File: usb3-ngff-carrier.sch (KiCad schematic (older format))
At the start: 44 parts, among them J1 692221030100, J2 2199119-3, J3 Jack-DC, J4 693043020611, J5 Conn_01x03_Male, SW1 KMR221GLFS, U1 TPS82130SILR

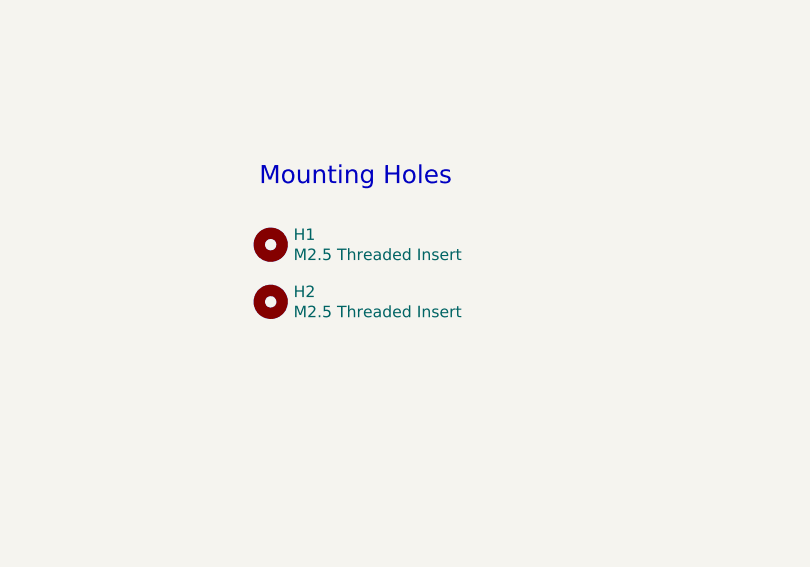
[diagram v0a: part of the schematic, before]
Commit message: Change: SIM holder
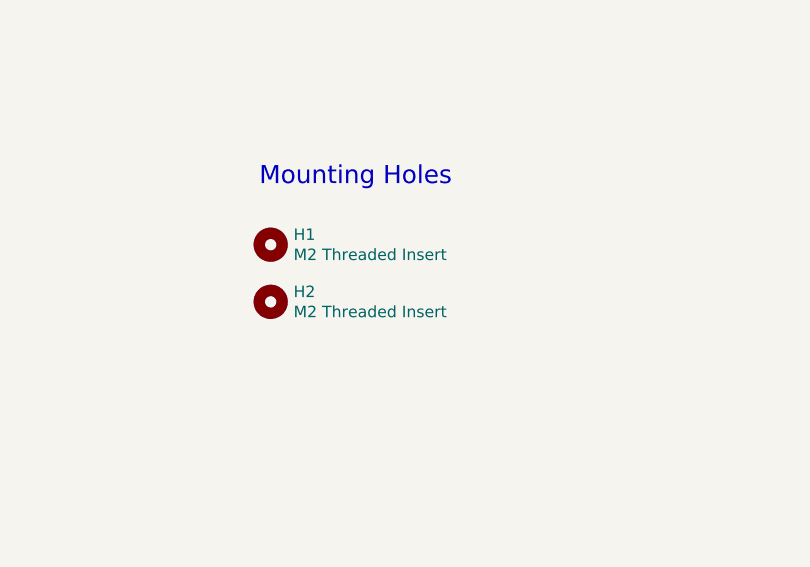
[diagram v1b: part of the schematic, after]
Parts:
- H1, H2: value M2.5 Threaded Insert -> M2 Threaded Insert
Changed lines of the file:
@@
 P 5200 3750
 F 0 "H1" H 5300 3794 50  0000 L CNN
-F 1 "M2.5 Threaded Insert" H 5300 3706 50  0000 L CNN
+F 1 "M2 Threaded Insert" H 5300 3706 50  0000 L CNN
 F 2 "footprint:9774015243RStandoff" H 5200 3750 50  0001 C CNN
 F 3 "https://www.mouser.co.uk/datasheet/2/445/9774015243R-1728818.pdf" H 5200 3750 50  0001 C CNN
@@
 P 5200 4000
 F 0 "H2" H 5300 4044 50  0000 L CNN
-F 1 "M2.5 Threaded Insert" H 5300 3956 50  0000 L CNN
+F 1 "M2 Threaded Insert" H 5300 3956 50  0000 L CNN
 F 2 "footprint:9774015243RStandoff" H 5200 4000 50  0001 C CNN
 F 3 "https://www.mouser.co.uk/datasheet/2/445/9774015243R-1728818.pdf" H 5200 4000 50  0001 C CNN

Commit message: Add: README, BOM and a few other bits
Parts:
- C4, C9: Note (none) -> Tantalum
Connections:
- wire segments 188 -> 182
- no-connect marks 55 -> 76
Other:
- note added: "Note"
- note added: "Some modules (RM500Q-GL) have the USB SS\nAC-coupling capacitors integrated. They are\nNOT present on this design for this reason.\n\nSome modules may require them. CHECK."
- note added: "USB traces must be routed in accordance with TUSB73x0.\nRecommend traces on back-side of board."
- moved on the sheet: C1, C14, C2, C3, D1, D2, H1, H2, J2, R2, R3, R5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

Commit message: Add: Rev2 changes
* Changed switcher to Diodes Inc device.
* Added second USIM slot and changed USIM slot part.
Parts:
- removed C17, C18, C19: 33pF, Capacitor_SMD:C_0402_1005Metric, symbol Device:C
- removed J4: 693043020611, footprint:Wurth-693043020611-MFG, symbol Wurth-693043020611~:693043020611
- removed R6, R7, R8: 22R, Resistor_SMD:R_0603_1608Metric, symbol Device:R
- removed TP3: PGOOD, TestPoint:TestPoint_Pad_D1.5mm, symbol Connector:TestPoint_Small
- removed U1: TPS82130SILR, footprint:Texas_Instruments-SIL0008D-0-0-0, symbol TPS82130SILR:TPS82130SILR
- added C15: 22uF, Capacitor_SMD:C_1210_3225Metric, symbol Device:C
- added C17, C18, C19, C21, C22, C23: 33pF, Capacitor_SMD:C_0603_1608Metric, symbol Device:C_Small
- added C20: 100nF, Capacitor_SMD:C_0603_1608Metric, symbol Device:C
- added J4, J6: SIM8060-6-1-14-00-A, GCT_SIM8060-6-1-14-00-A, symbol SIM8060-6-1-14-00-A:SIM8060-6-1-14-00-A
- added L1: 2.2uH, Inductor_SMD:L_Coilcraft_XAL5030, symbol Device:L
- added R10, R11, R12, R6, R7, R8: 22R, Resistor_SMD:R_0603_1608Metric, symbol Device:R_Small
- added U1: AP62301WU7, Package_TO_SOT_SMD:TSOT-23-6, symbol Power_Management:AP62301WU7
- C1: Int @ 10 0.106 -> 0.059; MPN JMF212AB7106KGHT -> GRM21BR71A106KA73K; Mfr Taiyo-Yuden -> MuRata Electronics; SKU 963-JMF212AB7106KGHT -> 81-GRM21BR71A106KA73K
- C10, C5: Int @ 10 0.077 -> 0.035; MPN C0603C105K9RAC7411 -> CGA3E1X7R1C105K080AC; Mfr KEMET -> TDK; SKU 80-C0603C105K9R7411 -> 810-CGA3E1X7R1C105K080AC
- C11, C16, C6: footprint Capacitor_SMD:C_0402_1005Metric -> Capacitor_SMD:C_0603_1608Metric; Int @ 10 0.039 -> 0.069; MPN C0402C104K9RACAUTO -> C0603C104K3RAC; SKU 80-C0402C104K9RAUTO -> 80-C0603C104K3RAC
- C12, C14, C7: footprint Capacitor_SMD:C_0402_1005Metric -> Capacitor_SMD:C_0603_1608Metric; Int @ 10 0.038 -> 0.023; MPN GRM0225C1H330JA02L -> 06035A330KAT2A; Mfr MuRata Electronics -> AVX; SKU 81-GRM0225C1H330JA2L -> 581-06035A330KAT2A
- C13, C8: footprint Capacitor_SMD:C_0402_1005Metric -> Capacitor_SMD:C_0603_1608Metric; Int @ 10 0.031 -> 0.023; MPN TMK042CG100DD-W -> 06035A100JAT4A; Mfr Taiyo-Yuden -> AVX; SKU 963-TMK042CG100DD-W -> 581-06035A100JAT4A
- C2: value 430pF -> 100nF; footprint Capacitor_SMD:C_0402_1005Metric -> Capacitor_SMD:C_0603_1608Metric; Int @ 10 0.206 -> 0.069; MPN C0402C431J5GACTU -> C0603C104K3RAC; SKU 80-C0402C431J5GACTU -> 80-C0603C104K3RAC
- C4, C9: Int @ 10 0.703 -> 0.499; MPN 6TPE100MZB -> TCJB107M006R0040; Mfr Panasonic -> AVX; SKU 667-6TPE100MZB -> 581-TCJB107M006R0040
- J1: value 692221030100 -> KUSBX-BS1N9-1-BL30; Int @ 10 2.79 -> 1.75; MPN 692221030100 -> KUSBX-BS1N9-1-BL30; Mfr Wurth -> Kycon; SKU 710-692221030100 -> 806-KUSBX-BS1N91BL30
- R2: value 100k -> 0R
- R3: value 374k -> 10k
- R5: value 100k -> 36k5; Int @ 10 (none) -> 0.023; MPN (none) -> CRCW060336K5FKEA; Mfr (none) -> Vishay; SKU (none) -> 71-CRCW060336K5FKEA; Vendor (none) -> Mouser
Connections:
- net labels added: RFFE_VIO_1V8, SW
- net labels removed: REFE_VIO_1V8
- wire segments 182 -> 204
- no-connect marks 76 -> 70
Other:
- note added: "Buck Converter"
- note added: "Dual Nano-SIM Holders"
- note added: "Some modules (RM500Q-GL) have the USB SS\nAC-coupling capacitors integrated. They are\nNOT present on this design for this reason.\n\nSome modules may require them. CHECK.\n\nADDITIONALLY - Note that the TX-RX pairing flips here."
- note removed: "4FF Nano-SIM Holder"
- note removed: "DC-DC (~~6V -> 3.8V)"
- note removed: "Some modules (RM500Q-GL) have the USB SS\nAC-coupling capacitors integrated. They are\nNOT present on this design for this reason.\n\nSome modules may require them. CHECK."
- moved on the sheet: C1, C10, C11, C12, C13, C14, C4, C5, C6, C7, C8, C9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
